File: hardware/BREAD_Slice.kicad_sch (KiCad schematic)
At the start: 36 parts, among them J10 Screw_Terminal_01x02, J11 Screw_Terminal_01x02, J12 Screw_Terminal_01x02, J15 Screw_Terminal_01x02, J16 Screw_Terminal_01x02, J17 Screw_Terminal_01x02, J5 Screw_Terminal_01x02, J6 Screw_Terminal_01x02, J7 Screw_Terminal_01x02, J8 Screw_Terminal_01x02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

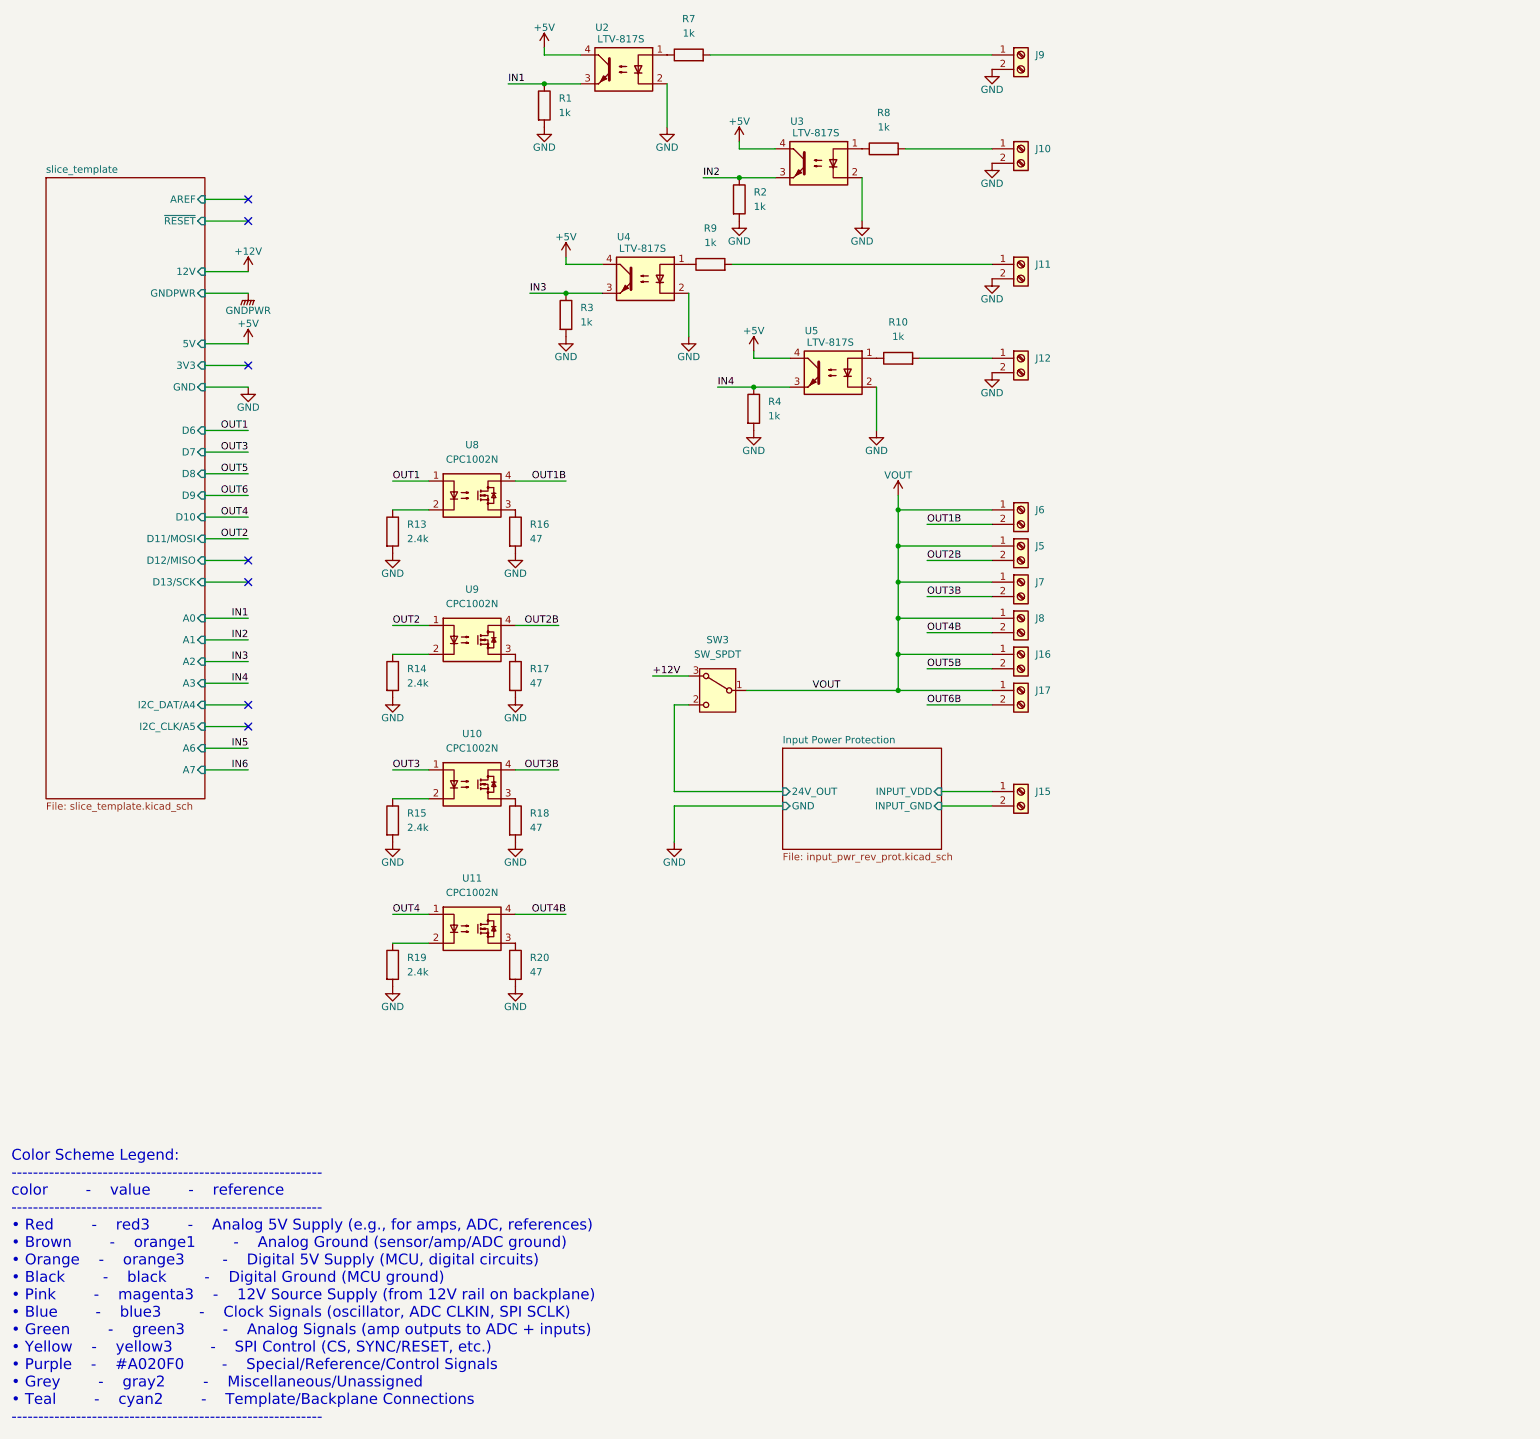
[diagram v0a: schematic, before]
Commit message: further revision of schem, add subsheets
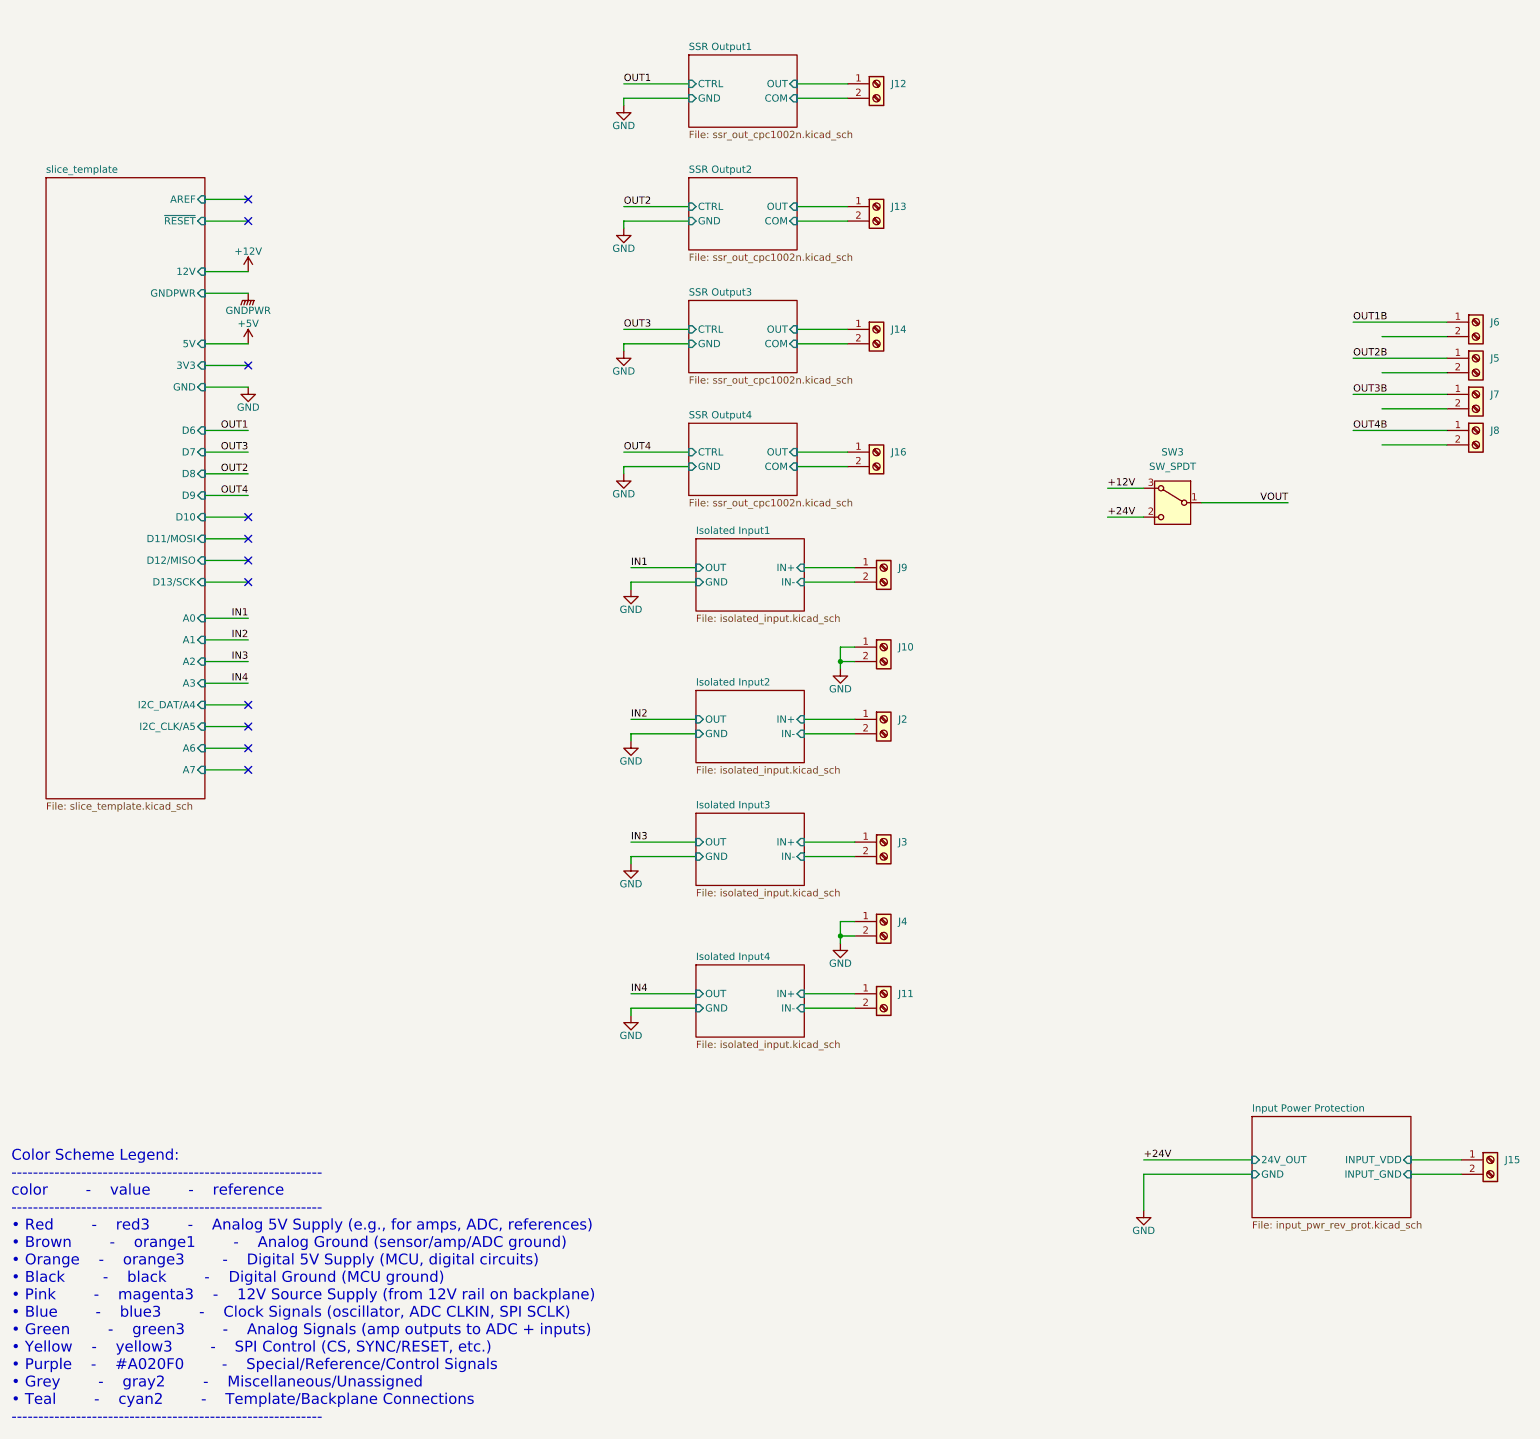
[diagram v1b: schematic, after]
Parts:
- removed J17: Screw_Terminal_01x02, symbol Connector:Screw_Terminal_01x02
- removed R1, R10, R2, R3, R4, R7, R8, R9: 1k, Resistor_SMD:R_0603_1608Metric, symbol Device:R
- removed R13, R14, R15, R19: 2.4k, Resistor_SMD:R_0603_1608Metric, symbol Device:R
- removed R16, R17, R18, R20: 47, Resistor_SMD:R_0603_1608Metric, symbol Device:R
- removed U10, U11, U8, U9: CPC1002N, Package_SO:SOP-4_3.8x4.1mm_P2.54mm, symbol Relay_SolidState:CPC1002N
- removed U2, U3, U4, U5: LTV-817S, Package_DIP:SMDIP-4_W9.53mm, symbol Isolator:LTV-817S
- added J13, J14, J2, J3, J4: Screw_Terminal_01x02, symbol Connector:Screw_Terminal_01x02
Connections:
- net GND: now also J10.1 (Pin_1), J4.1 (Pin_1), J4.2 (Pin_2); no longer J11.2 (Pin_2), J12.2 (Pin_2), J9.2 (Pin_2)
- net OUT1B: now also J6.1 (Pin_1); no longer J6.2 (Pin_2)
- net OUT2B: now also J5.1 (Pin_1); no longer J5.2 (Pin_2)
- net OUT3B: now also J7.1 (Pin_1); no longer J7.2 (Pin_2)
- net OUT4B: now also J8.1 (Pin_1); no longer J8.2 (Pin_2)
- net VOUT: no longer J16.1 (Pin_1), J5.1 (Pin_1), J6.1 (Pin_1), J7.1 (Pin_1), J8.1 (Pin_1)
- net Isolated Input1/IN+: now reaches J9.1 (Pin_1)
- net Isolated Input4/IN+: now reaches J11.1 (Pin_1)
- net SSR Output1/OUT: now reaches J12.1 (Pin_1)
- net Input Power Protection/24V_OUT renamed +24V
- net OUT5B renamed SSR Output4/COM
- new net Isolated Input1/IN-: J9.2 (Pin_2)
- new net Isolated Input2/IN+: J2.1 (Pin_1)
- new net Isolated Input2/IN-: J2.2 (Pin_2)
- new net Isolated Input3/IN+: J3.1 (Pin_1)
- new net Isolated Input3/IN-: J3.2 (Pin_2)
- new net Isolated Input4/IN-: J11.2 (Pin_2)
- new net SSR Output1/COM: J12.2 (Pin_2)
- new net SSR Output2/COM: J13.2 (Pin_2)
- new net SSR Output2/OUT: J13.1 (Pin_1)
- new net SSR Output3/COM: J14.2 (Pin_2)
- new net SSR Output3/OUT: J14.1 (Pin_1)
- new net SSR Output4/OUT: J16.1 (Pin_1)
- no-connect marks 7 -> 11
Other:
- added sheet Isolated Input1 (isolated_input.kicad_sch)
- added sheet Isolated Input2 (isolated_input.kicad_sch)
- added sheet Isolated Input3 (isolated_input.kicad_sch)
- added sheet Isolated Input4 (isolated_input.kicad_sch)
- added sheet SSR Output1 (ssr_out_cpc1002n.kicad_sch)
- added sheet SSR Output2 (ssr_out_cpc1002n.kicad_sch)
- added sheet SSR Output3 (ssr_out_cpc1002n.kicad_sch)
- added sheet SSR Output4 (ssr_out_cpc1002n.kicad_sch)
- moved on the sheet: J10, J15, J5, J6, J7, J8, J9, SW3
